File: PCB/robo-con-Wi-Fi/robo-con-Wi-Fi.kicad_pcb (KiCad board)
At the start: 4 copper layers, 86 x 67 mm, 94 parts, among them J1 Conn_01x04, J2 SMA-J, J3 Conn_01x05, J5 Conn_01x02, J7 Conn_01x06, SW1 SW_Push, SW2 SW_Push, U1 STM32H723VGTx, U10 MCP73831-2-OT, U11 LM66100DCK, U12 NJM12877, U13 TXB0606DYYR, U18 USB_Type-C, U2 LBEE5HY2FY, U3 TXU0204, U4 IS25LP128-JBLE, U5 RKJXV122400R, U6 NJM2884U1-33, U7 RKJXV122400R, U8 TMHU28, U9 TMHU28

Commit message: RF部の配線
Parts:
- removed C26: 0.33u, Capacitor_SMD:C_0402_1005Metric_Pad0.74x0.62mm_HandSolder
- removed C29: 2.2u, Capacitor_SMD:C_0402_1005Metric_Pad0.74x0.62mm_HandSolder
- removed R79: 1k, Resistor_SMD:R_0402_1005Metric_Pad0.72x0.64mm_HandSolder
- removed U6: NJM2884U1-33, Package_TO_SOT_SMD:SOT-89-5
- added C32: 0.1uF, Capacitor_SMD:C_0402_1005Metric_Pad0.74x0.62mm_HandSolder, F.Cu at (95.1, 85.3)
- added C86: 0.1u, Capacitor_SMD:C_0402_1005Metric_Pad0.74x0.62mm_HandSolder, F.Cu at (55.9, 72.1)
- added C87: 4.7u, Capacitor_SMD:C_0402_1005Metric_Pad0.74x0.62mm_HandSolder, F.Cu at (55.9, 74.1)
- added D4: MS18F, Diode_SMD:D_2010_5025Metric_Pad1.52x2.65mm_HandSolder, F.Cu at (190.0, 66.7)
- added J4: Conn_01x01, Connector_Wire:SolderWirePad_1x01_SMD_1.5x3mm, F.Cu at (210.4, 50.4)
- added J6: Conn_01x01, Connector_Wire:SolderWirePad_1x01_SMD_1.5x3mm, F.Cu at (199.6, 39.5)
- added R51: WA04X102, My_Library:WA04X102, F.Cu at (94.0, 51.7)
- added R52: WA04X102, My_Library:WA04X102, F.Cu at (94.0, 54.0)
- added U14: TPS628513DRLR, Package_TO_SOT_SMD:SOT-583-8, F.Cu at (189.2, 54.3)
- added U17: ~, My_Library:ECS-TXO-2520-33-500-AN-TR, F.Cu at (95.7, 82.3)
- J1: footprint Connector_PinSocket_2.54mm:PinSocket_1x04_P2.54mm_Vertical -> Connector_PinSocket_2.54mm:PinSocket_1x04_P2.54mm_Horizontal
- J2: footprint Connector_Coaxial:SMA_Samtec_SMA-J-P-H-ST-EM1_EdgeMount -> My_Library:SMA_Conn
- J5: moved to F.Cu
- R12: footprint Resistor_SMD:R_0603_1608Metric_Pad0.98x0.95mm_HandSolder -> Resistor_SMD:R_0402_1005Metric_Pad0.72x0.64mm_HandSolder
- R24: footprint Resistor_SMD:R_0402_1005Metric_Pad0.72x0.64mm_HandSolder -> Resistor_SMD:R_0603_1608Metric_Pad0.98x0.95mm_HandSolder
- moved U11 127.8 mm to (194.6, 52.9), turned to -90 degrees
- moved J3 116.3 mm to (205.3, 62.5), turned to 90 degrees
- moved R78 116.2 mm to (198.6, 45.4)
- moved R77 116.1 mm to (198.6, 44.4)
- moved FB1 115.2 mm to (198.3, 51.2), turned to -90 degrees
- moved D12 113.0 mm to (182.9, 67.7), turned to 90 degrees
- moved C6 110.0 mm to (196.6, 49.8), turned to 90 degrees
- moved C12 110.0 mm to (196.6, 52.6), turned to -90 degrees
- moved C13 108.0 mm to (194.7, 55.4), turned to 180 degrees
- moved R24 104.9 mm to (184.8, 61.8), turned to 90 degrees
- moved R25 104.1 mm to (183.5, 70.3)
- moved U10 90.7 mm to (185.8, 66.7), turned to 90 degrees
- moved C62 90.4 mm to (186.8, 62.8), turned to 90 degrees
- moved C63 89.9 mm to (186.2, 70.0), turned to 180 degrees
- moved R12 88.4 mm to (145.5, 45.9)
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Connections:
- net ST_LED_4 renamed ST_LED_BOOT
- net VBUS renamed Net-(U11-VIN)
- C84 pad 1: +3.3V -> +1V8
- C85 pad 1: +1V8 -> +3.3V
- U1 pad 12: unconnected-(U1-PH0-Pad12) -> OSC
- U1 pad 65: unconnected-(U1-PC8-Pad65) -> SDMMC1_D0
- U1 pad 66: unconnected-(U1-PC9-Pad66) -> SDMMC1_D1
- U1 pad 78: unconnected-(U1-PC10-Pad78) -> SDMMC1_D2
- U1 pad 79: unconnected-(U1-PC11-Pad79) -> SDMMC1_D3
- U1 pad 80: unconnected-(U1-PC12-Pad80) -> SDMMC1_CLK
- U1 pad 83: unconnected-(U1-PD2-Pad83) -> SDMMC1_CMD
- U13 pad 10: SDMMC1_D3 -> SDMMC1_D0
- U13 pad 11: SDMMC1_D2 -> SDMMC1_CMD
- U13 pad 13: SDMMC1_D0 -> SDMMC1_D2
- U13 pad 14: SDMMC1_CMD -> SDMMC1_D3
- U13 pad 3: Wi-Fi_CMD -> Wi-Fi_D3
- U13 pad 4: Wi-Fi_D0 -> Wi-Fi_D2
- U13 pad 6: Wi-Fi_D2 -> Wi-Fi_CMD
- U13 pad 7: Wi-Fi_D3 -> Wi-Fi_D0
- U2 pad 1: unconnected-(U2-GPIO_6-Pad1) -> WL-GPIO_6
- U2 pad 2: unconnected-(U2-GPIO_0-Pad2) -> WL-GPIO_0
- U2 pad 3: unconnected-(U2-GPIO_3-Pad3) -> WL-GPIO_3
- U2 pad 4: unconnected-(U2-GPIO_5-Pad4) -> WL-GPIO_5
- U2 pad 5: unconnected-(U2-LHL_GPIO_1-Pad5) -> LHL_GPIO_1
- U2 pad 6: unconnected-(U2-GPIO_4-Pad6) -> WL-GPIO_4
- U2 pad 7: unconnected-(U2-GPIO_2-Pad7) -> WL-GPIO_2
- U3 pad 1: +1V8 -> +3.3V
- U3 pad 11: +3.3V -> +1V8
- U3 pad 12: +1V8 -> +3.3V
- U4 pad 1: unconnected-(U4-CE#-Pad1) -> SPI1_NSS
- U4 pad 2: unconnected-(U4-SO(IO1)-Pad2) -> SPI1_MISO
- U4 pad 3: unconnected-(U4-WP#(IO2)-Pad3) -> WP
- U4 pad 4: unconnected-(U4-GND-Pad4) -> GND
- U4 pad 5: unconnected-(U4-SI(IS0)-Pad5) -> SPI1_MOSI
- U4 pad 6: unconnected-(U4-SCK-Pad6) -> SPI1_SCK
- U4 pad 7: unconnected-(U4-HOLD#(IO3)-Pad7) -> HOLD
- U4 pad 8: unconnected-(U4-VCC-Pad8) -> +3.3V
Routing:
- net +5V: track 0.00 -> 25.7 mm
- net +3.3V: track 0.00 -> 17.6 mm
- net Net-(C6-Pad1): track 0.00 -> 13.8 mm, vias 0 -> 2
- net Net-(U18-CC2): track 0.00 -> 10.4 mm
- net +BATT: track 0.00 -> 8.32 mm
- net +1V8: track 0.00 -> 7.16 mm
- net BT_UART_CTS: track 0.00 -> 6.87 mm
- net BT_UART_RTS: track 0.00 -> 6.82 mm
- net BT_UART_RX: track 0.00 -> 6.78 mm
- net BT_UART_TX: track 0.00 -> 6.74 mm
- net Net-(U18-CC1): track 0.00 -> 6.64 mm
- net Net-(J2-In): track 7.54 -> 13.3 mm
- net Wi-Fi_D3: track 0.00 -> 4.12 mm
- net Wi-Fi_D2: track 0.00 -> 4.12 mm
- net Wi-Fi_D1: track 0.00 -> 4.12 mm
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- added copper zone on B.Cu, net GND
- added copper zone on F.Cu, net GND
- added copper zone on In1.Cu, net GND
- added copper zone on In2.Cu, net GND
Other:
- outline, holes or cut-outs redrawn
- board text added: "+5V"
- board text added: "BOOT/USB"
- board text added: "GND"
- board text added: "LiPo"
- board text added: "NRST"

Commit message: 電源周りの部品構成完了
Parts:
- removed D4: MS18F, Diode_SMD:D_2010_5025Metric_Pad1.52x2.65mm_HandSolder
- removed R35, R36: 1k, Resistor_SMD:R_0402_1005Metric_Pad0.72x0.64mm_HandSolder
- removed R51, R52: WA04X102, My_Library:WA04X102
- added C14: 0.1u, Capacitor_SMD:C_0402_1005Metric_Pad0.74x0.62mm_HandSolder, F.Cu at (189.6, 69.0)
- added C15: 0.1u, Capacitor_SMD:C_0402_1005Metric_Pad0.74x0.62mm_HandSolder, F.Cu at (189.6, 64.5)
- added C88: 10u, Capacitor_SMD:C_0603_1608Metric_Pad1.08x0.95mm_HandSolder, F.Cu at (120.7, 64.5)
- added C89: 10u, Capacitor_SMD:C_0603_1608Metric_Pad1.08x0.95mm_HandSolder, F.Cu at (120.7, 67.0)
- added C90: 2.2u, Capacitor_SMD:C_0402_1005Metric_Pad0.74x0.62mm_HandSolder, F.Cu at (106.8, 87.1)
- added C91: 10u, Capacitor_SMD:C_0603_1608Metric_Pad1.08x0.95mm_HandSolder, F.Cu at (120.7, 69.5)
- added C92: 10u, Capacitor_SMD:C_0603_1608Metric_Pad1.08x0.95mm_HandSolder, F.Cu at (120.7, 72.0)
- added C93: 1u, Capacitor_SMD:C_0402_1005Metric_Pad0.74x0.62mm_HandSolder, F.Cu at (124.5, 70.2)
- added C94: 10p, Capacitor_SMD:C_0402_1005Metric_Pad0.74x0.62mm_HandSolder, F.Cu at (124.5, 72.1)
- added C95: 2.2u, Capacitor_SMD:C_0402_1005Metric_Pad0.74x0.62mm_HandSolder, F.Cu at (106.8, 89.1)
- added L2: 0.47u, Inductor_SMD:L_0603_1608Metric_Pad1.05x0.95mm_HandSolder, F.Cu at (120.7, 74.5)
- added Q1: 2SC3325-Y, Package_TO_SOT_SMD:SC-59, F.Cu at (90.2, 65.8)
- added R3: 2.2k, Resistor_SMD:R_0402_1005Metric_Pad0.72x0.64mm_HandSolder, F.Cu at (94.3, 64.3)
- added R39: 10k, Resistor_SMD:R_0402_1005Metric_Pad0.72x0.64mm_HandSolder, F.Cu at (94.3, 66.3)
- added R40: 88.7k, Resistor_SMD:R_0402_1005Metric_Pad0.72x0.64mm_HandSolder, F.Cu at (124.5, 64.2)
- added R41: 19.6k, Resistor_SMD:R_0402_1005Metric_Pad0.72x0.64mm_HandSolder, F.Cu at (124.5, 66.2)
- added R42: 100k, Resistor_SMD:R_0402_1005Metric_Pad0.72x0.64mm_HandSolder, F.Cu at (124.5, 68.2)
- added U15: LM66100DCK, Package_TO_SOT_SMD:SOT-363_SC-70-6, F.Cu at (189.6, 66.8)
- added U6: IS25LP064D-JLLE, Package_SON:WSON-8-1EP_8x6mm_P1.27mm_EP3.4x4.3mm, F.Cu at (180.0, 56.0)
- L1: footprint Capacitor_SMD:C_0402_1005Metric_Pad0.74x0.62mm_HandSolder -> Inductor_SMD:L_1008_2520Metric_Pad1.43x2.20mm_HandSolder
- U4: value IS25LP128-JBLE -> MCP1792x-3302xCB; footprint Package_SO:SOIC-8_5.3x5.3mm_P1.27mm -> Package_TO_SOT_SMD:SOT-23
- moved U4 85.2 mm to (102.8, 88.3)
- moved C77 46.8 mm to (149.2, 54.4)
- moved L1 32.2 mm to (151.4, 56.4)
- moved C76 2.08 mm to (146.0, 53.8)
- moved C75 2.08 mm to (146.0, 52.7)
- moved U1 1.10 mm to (168.0, 73.2)
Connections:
- C32 pad 1: +3.3V -> OSC_3.3v
- R32 pad 1: ST_LED_BOOT -> ST_LED_4
- R34 pad 1: ST_LED_W5500 -> ST_LED_BOOT
- U1 pad 15: unconnected-(U1-PC0-Pad15) -> SPI1_MOSI/QSPI1_IO0
- U1 pad 16: unconnected-(U1-PC1-Pad16) -> SPI1_MISO/QSPI1_IO1
- U1 pad 17: unconnected-(U1-PC2_C-Pad17) -> WP/QSPI1_IO2
- U1 pad 25: unconnected-(U1-PA3-Pad25) -> SPI1_SCK/QSPI1_SCK
- U1 pad 40: unconnected-(U1-PE10-Pad40) -> HOLD/QSPI1_IO3
- U1 pad 41: unconnected-(U1-PE11-Pad41) -> SPI1_NSS/QSPI1_NSS
- U1 pad 84: unconnected-(U1-PD3-Pad84) -> UART1_CTS
- U1 pad 85: unconnected-(U1-PD4-Pad85) -> UART1_RTS
- U1 pad 86: unconnected-(U1-PD5-Pad86) -> UART1_TX
- U1 pad 87: unconnected-(U1-PD6-Pad87) -> UART1_RX
- U1 pad 95: unconnected-(U1-PB8-Pad95) -> SDMMC1_CLKIN
- U14 pad 1: unconnected-(U14-VIN-Pad1) -> +5V
- U14 pad 2: unconnected-(U14-EN-Pad2) -> +5V
- U14 pad 3: unconnected-(U14-MODE-Pad3) -> +5V
- U14 pad 4: unconnected-(U14-SS/TR-Pad4) -> Net-(U14-SS/TR)
- U14 pad 5: unconnected-(U14-FB-Pad5) -> Net-(U14-FB)
- U14 pad 6: unconnected-(U14-PG-Pad6) -> Net-(U14-PG)
- U14 pad 7: unconnected-(U14-SW-Pad7) -> Net-(U14-SW)
- U14 pad 8: unconnected-(U14-GND-Pad8) -> GND
- U17 pad 1: +3.3V -> OSC_3.3v
- U17 pad 4: +3.3V -> OSC_3.3v
- U2 pad 1: WL-GPIO_6 -> unconnected-(U2-GPIO_6-Pad1)
- U2 pad 2: WL-GPIO_0 -> WL_HOST_WAKE
- U2 pad 3: WL-GPIO_3 -> unconnected-(U2-GPIO_3-Pad3)
- U2 pad 4: WL-GPIO_5 -> unconnected-(U2-GPIO_5-Pad4)
- U2 pad 40: Net-(U2-LHL_GPIO_0) -> BT_DEV_WAKE
- U2 pad 41: Net-(U2-BT_HOST_WAKE) -> BT_HOST_WAKE
- U2 pad 5: LHL_GPIO_1 -> WL_DEV_WAKE
- U2 pad 6: WL-GPIO_4 -> unconnected-(U2-GPIO_4-Pad6)
- U2 pad 7: WL-GPIO_2 -> unconnected-(U2-GPIO_2-Pad7)
- U4 pad 1: SPI1_NSS -> GND
- U4 pad 2: SPI1_MISO -> OSC_3.3v
- U4 pad 3: WP -> +5V
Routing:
- net +3.3V: track 17.6 -> 10.5 mm
- net Net-(U2-BT_HOST_WAKE): track 2.65 -> 0.00 mm
- net BT_HOST_WAKE: track 0.00 -> 2.65 mm
- net +BATT: track 8.32 -> 10.3 mm
- net BT_DEV_WAKE: track 0.00 -> 1.83 mm

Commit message: PCB
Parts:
- removed C32: 0.1uF, Capacitor_SMD:C_0402_1005Metric_Pad0.74x0.62mm_HandSolder
- removed C90, C95: 2.2u, Capacitor_SMD:C_0402_1005Metric_Pad0.74x0.62mm_HandSolder
- removed U17: ~, My_Library:ECS-TXO-2520-33-500-AN-TR
- removed U4: MCP1792x-3302xCB, Package_TO_SOT_SMD:SOT-23
- added C34: 18pF, Capacitor_SMD:C_0402_1005Metric_Pad0.74x0.62mm_HandSolder, F.Cu at (158.4, 77.1)
- added C35: 18pF, Capacitor_SMD:C_0402_1005Metric_Pad0.74x0.62mm_HandSolder, F.Cu at (158.4, 74.7)
- added R43: 1k, Resistor_SMD:R_0402_1005Metric_Pad0.72x0.64mm_HandSolder, F.Cu at (159.6, 54.6)
- added Y2: XRCGB25M000FFS1AR0, My_Library:XRCGB25M000FFS1AR0, F.Cu at (157.3, 76.1)
- R23: footprint Resistor_SMD:R_0603_1608Metric_Pad0.98x0.95mm_HandSolder -> Resistor_SMD:R_0402_1005Metric_Pad0.72x0.64mm_HandSolder
- moved R31 125.2 mm to (197.5, 32.1)
- moved R28 121.9 mm to (197.4, 92.8)
- moved C86 119.8 mm to (174.8, 57.8), turned to -90 degrees
- moved R30 118.9 mm to (193.5, 27.8)
- moved C87 118.7 mm to (173.5, 57.8), turned to -90 degrees
- moved C89 78.6 mm to (198.7, 57.4), turned to 90 degrees
- moved C50 78.1 mm to (180.9, 69.9)
- moved C31 77.9 mm to (180.9, 68.7)
- moved C88 76.8 mm to (197.1, 57.4), turned to 90 degrees
- moved C30 75.5 mm to (176.8, 87.3)
- moved C33 74.6 mm to (176.8, 86.0)
- moved C93 73.7 mm to (196.5, 55.0)
- moved C70 72.8 mm to (179.0, 85.3), turned to -90 degrees
- moved L2 72.4 mm to (191.1, 57.8), turned to 180 degrees
- moved R29 72.3 mm to (144.5, 94.6)
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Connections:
- U1 pad 12: OSC -> HSE_IN
- U1 pad 13: unconnected-(U1-PH1-Pad13) -> HSE_OUT
- U2 pad 2: WL_HOST_WAKE -> unconnected-(U2-GPIO_0-Pad2)
- U2 pad 40: BT_DEV_WAKE -> Net-(U2-LHL_GPIO_0)
- U2 pad 41: BT_HOST_WAKE -> unconnected-(U2-BT_HOST_WAKE-Pad41)
- U2 pad 5: WL_DEV_WAKE -> unconnected-(U2-LHL_GPIO_1-Pad5)
- U3 pad 10: BT_UART_TX -> BT_UART_RX
- U3 pad 2: UART1_RX -> UART1_TX
- U3 pad 3: UART1_TX -> UART1_RTS
- U3 pad 4: UART1_CTS -> UART1_RX
- U3 pad 5: UART1_RTS -> UART1_CTS
- U3 pad 7: BT_UART_CTS -> BT_UART_RTS
- U3 pad 8: BT_UART_RTS -> BT_UART_TX
- U3 pad 9: BT_UART_RX -> BT_UART_CTS
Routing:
- net SDMMC1_D0: track 0.00 -> 60.9 mm, vias 0 -> 2
- net SDMMC1_D1: track 0.00 -> 57.8 mm, vias 0 -> 2
- net SDMMC1_CMD: track 0.00 -> 53.7 mm, vias 0 -> 2
- net SDMMC1_D2: track 0.00 -> 52.9 mm, vias 0 -> 2
- net SDMMC1_D3: track 0.00 -> 50.2 mm, vias 0 -> 2
- net SDMMC1_CLK: track 0.00 -> 48.7 mm, vias 0 -> 2
- net +3.3V: track 10.5 -> 51.1 mm
- net SPI1_SCK/QSPI1_SCK: track 0.00 -> 37.1 mm, vias 0 -> 2
- net WP/QSPI1_IO2: track 0.00 -> 35.2 mm, vias 0 -> 2
- net SPI1_MISO/QSPI1_IO1: track 0.00 -> 34.8 mm, vias 0 -> 2
- net HOLD/QSPI1_IO3: track 0.00 -> 33.8 mm, vias 0 -> 2
- net SPI1_MOSI/QSPI1_IO0: track 0.00 -> 33.4 mm, vias 0 -> 2
- net USB_DFU_DN: track 2.70 -> 35.7 mm, vias 0 -> 2
- net USB_DFU_DP: track 2.70 -> 35.6 mm, vias 0 -> 2
- net SPI1_NSS/QSPI1_NSS: track 0.00 -> 31.3 mm, vias 0 -> 2
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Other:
- board text added: "BOOT0"
- board text removed: "BOOT/USB"

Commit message: LEDを置く位置が微妙い
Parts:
- moved D1 38.3 mm to (107.8, 60.4)
- moved D10 38.3 mm to (107.8, 68.2)
- moved D11 38.3 mm to (107.8, 70.7)
- moved D13 38.3 mm to (107.8, 75.9)
- moved D14 38.3 mm to (107.8, 78.5)
- moved D15 38.3 mm to (107.8, 81.1)
- moved D3 38.3 mm to (107.8, 63.0)
- moved D5 38.3 mm to (107.8, 65.6)
- moved R11 38.3 mm to (114.9, 60.1)
- moved R2 38.3 mm to (111.6, 60.1)
- moved R21 38.3 mm to (114.9, 72.0)
- moved R32 38.3 mm to (118.2, 70.0)
- moved R33 38.3 mm to (118.2, 72.0)
- moved R34 38.3 mm to (121.4, 60.1)
- moved R4 38.3 mm to (111.6, 64.1)
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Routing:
- net NRST: track 0.00 -> 98.9 mm, vias 0 -> 2
- net SWCLK: track 0.00 -> 55.1 mm, vias 0 -> 2
- net SWDIO: track 0.00 -> 53.4 mm, vias 0 -> 1
- net SDMMC1_CLKIN: track 0.00 -> 30.6 mm
- net +1V8: track 30.4 -> 54.3 mm, vias 0 -> 2
- net BOOT0: track 0.00 -> 22.0 mm, vias 0 -> 2
- net SPI1_MOSI/QSPI1_IO0: track 33.4 -> 24.0 mm, vias 2 -> 1
- net SPI1_MISO/QSPI1_IO1: track 34.8 -> 26.0 mm, vias 2 -> 1
- net WP/QSPI1_IO2: track 35.2 -> 26.6 mm, vias 2 -> 1
- net SPI1_NSS/QSPI1_NSS: track 31.3 -> 27.5 mm
- net SPI1_SCK/QSPI1_SCK: track 37.1 -> 34.6 mm
- net +3.3V: track 51.1 -> 50.0 mm
- net HOLD/QSPI1_IO3: track 33.8 -> 33.3 mm

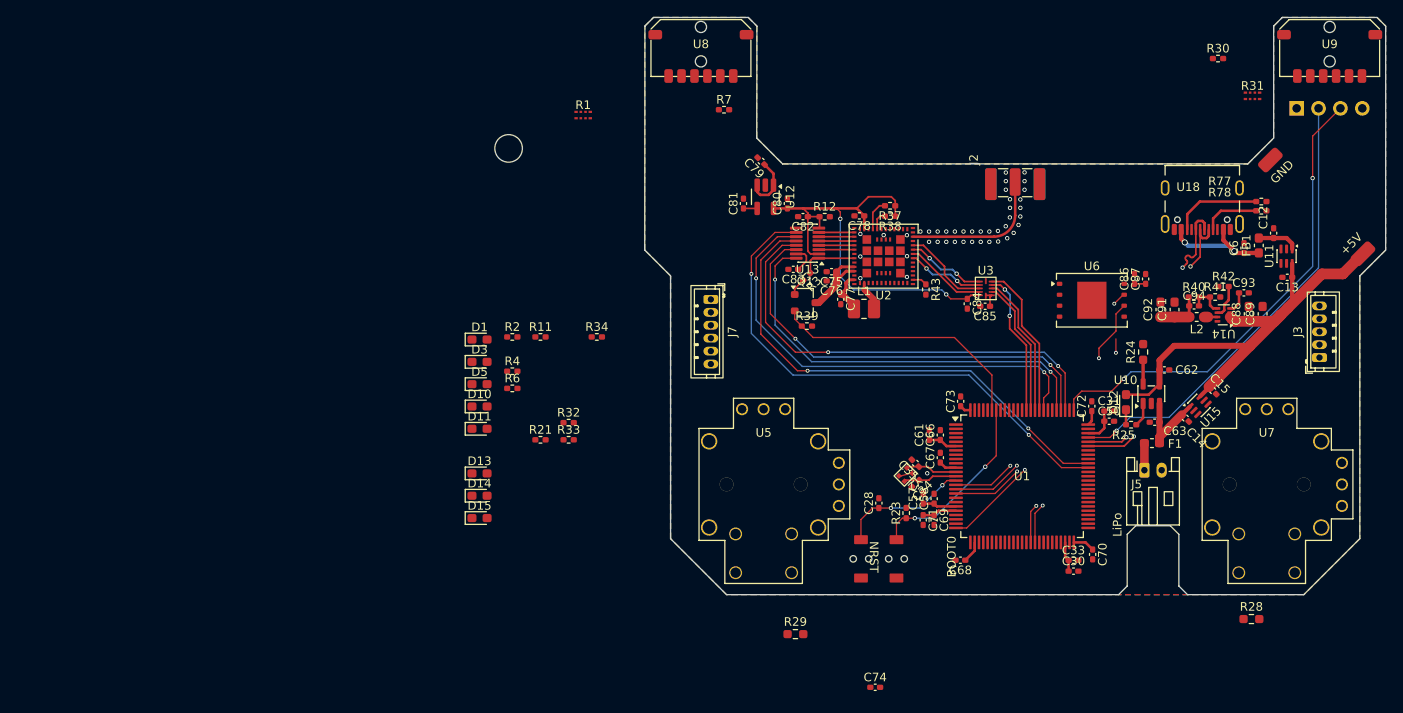
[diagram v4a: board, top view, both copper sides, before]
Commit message: LiPo監視用ADCとLED追加
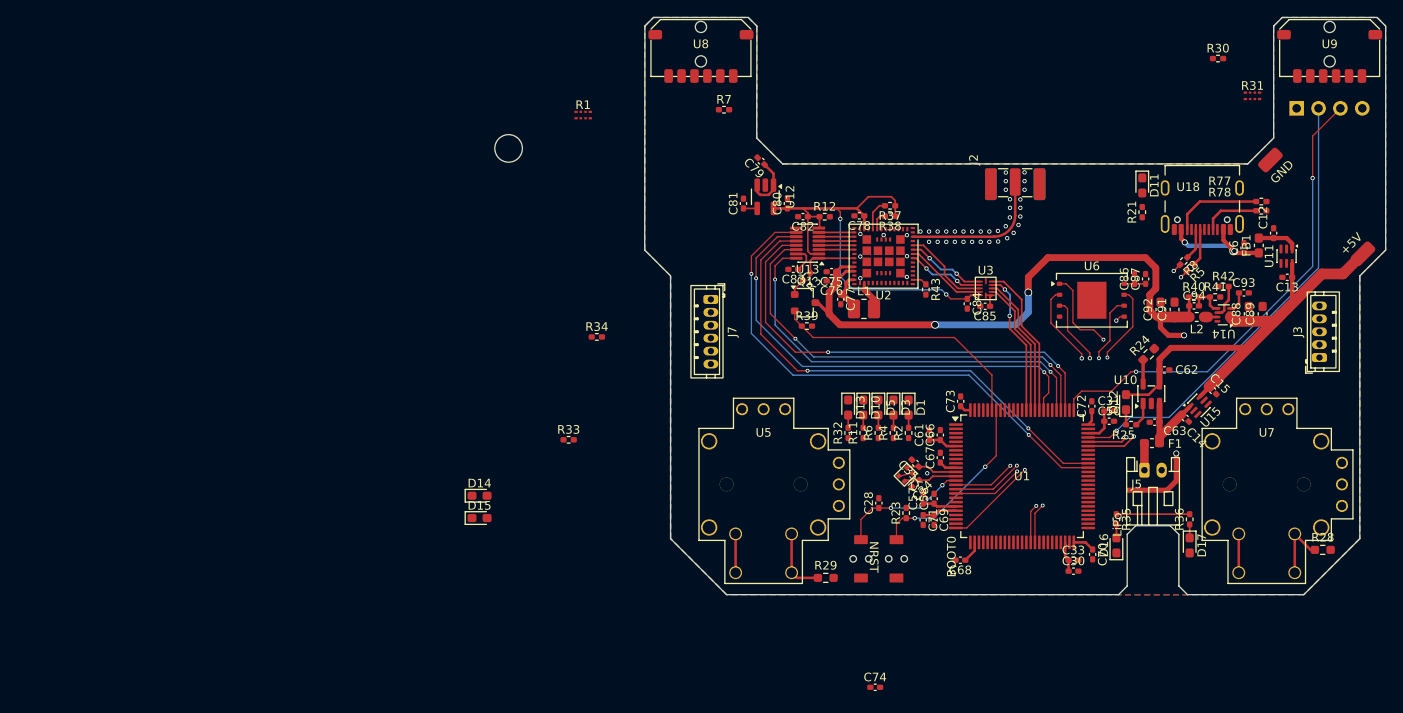
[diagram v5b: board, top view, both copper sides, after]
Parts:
- added D16: R, Diode_SMD:D_0603_1608Metric_Pad1.05x0.95mm_HandSolder, F.Cu at (181.8, 84.3)
- added D17: G, Diode_SMD:D_0603_1608Metric_Pad1.05x0.95mm_HandSolder, F.Cu at (190.3, 84.3)
- added R35: 1k, Resistor_SMD:R_0402_1005Metric_Pad0.72x0.64mm_HandSolder, F.Cu at (181.8, 81.3)
- added R36: 1k, Resistor_SMD:R_0402_1005Metric_Pad0.72x0.64mm_HandSolder, F.Cu at (190.3, 81.3)
- added R5: 22, Resistor_SMD:R_0402_1005Metric_Pad0.72x0.64mm_HandSolder, F.Cu at (190.3, 52.0)
- added R8: 22, Resistor_SMD:R_0402_1005Metric_Pad0.72x0.64mm_HandSolder, F.Cu at (189.6, 51.3)
- moved D11 81.9 mm to (184.8, 42.5), turned to -90 degrees
- moved R21 74.7 mm to (184.8, 45.6), turned to 90 degrees
- moved D1 50.4 mm to (157.6, 68.3), turned to -90 degrees
- moved D3 48.3 mm to (155.9, 68.3), turned to -90 degrees
- moved R2 47.3 mm to (157.6, 71.2), turned to 90 degrees
- moved D5 46.4 mm to (154.1, 68.3), turned to -90 degrees
- moved R4 44.8 mm to (155.9, 71.2), turned to 90 degrees
- moved D10 44.5 mm to (152.4, 68.3), turned to -90 degrees
- moved D13 43.5 mm to (150.6, 68.3), turned to -90 degrees
- moved R6 42.8 mm to (154.1, 71.2), turned to 90 degrees
- moved R11 39.1 mm to (152.4, 71.2), turned to 90 degrees
- moved R32 32.5 mm to (150.6, 71.2), turned to 90 degrees
- moved R28 11.5 mm to (205.7, 84.8)
- moved R29 7.42 mm to (148.0, 88.0)
- moved R24 0.70 mm to (185.5, 62.1), turned to 45 degrees
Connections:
- net Net-(J5-Pin_1) renamed LiPo_Observer
- net ST_LED_0 renamed LED_0
- net ST_LED_1 renamed LED_1
- net ST_LED_2 renamed LED_2
- net ST_LED_3 renamed LED_3
- net ST_LED_4 renamed LED_4
- net ST_LED_BOOT renamed LED_Wi-Fi
- net ST_LED_USB renamed LED_USB
- U18 pad A6: USB_DFU_DP -> Net-(R8-Pad1)
- U18 pad A7: USB_DFU_DN -> Net-(R5-Pad1)
- U18 pad B6: USB_DFU_DP -> Net-(R8-Pad1)
- U18 pad B7: USB_DFU_DN -> Net-(R5-Pad1)
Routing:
- net +3.3V: track 50.0 -> 144.8 mm, vias 0 -> 4
- net SPI1_NSS/QSPI1_NSS: track 27.5 -> 37.8 mm
- net LiPo_State: track 0.00 -> 8.50 mm
- net USB_DFU_DN: track 35.7 -> 27.5 mm
- net Left_Push_Stick: track 0.00 -> 7.80 mm
- net Right_Push_Stick: track 0.00 -> 7.60 mm
- net USB_DFU_DP: track 35.6 -> 28.1 mm
- net SPI1_MISO/QSPI1_IO1: track 26.0 -> 33.3 mm, vias 1 -> 2
- net SPI1_MOSI/QSPI1_IO0: track 24.0 -> 31.1 mm, vias 1 -> 2
- net WP/QSPI1_IO2: track 26.6 -> 32.8 mm, vias 1 -> 2
- net Net-(R5-Pad1): track 0.00 -> 4.30 mm
- net Net-(R8-Pad1): track 0.00 -> 3.64 mm
- net Net-(D16-A): track 0.00 -> 1.56 mm
- net Net-(D17-K): track 0.00 -> 1.56 mm
- net Net-(D5-A): track 0.00 -> 1.48 mm
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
